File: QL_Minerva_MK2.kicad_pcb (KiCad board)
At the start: 2 copper layers, 41.9 x 44.5 mm, 16 parts, among them J1 Conn_01x02_Pin, J2 Conn_01x05_Pin, U1 Socket to QL, U2 W27C512, U3 PCF8583P, U4 GAL16V8, U5 74LS133, Y1 32.768 kHz

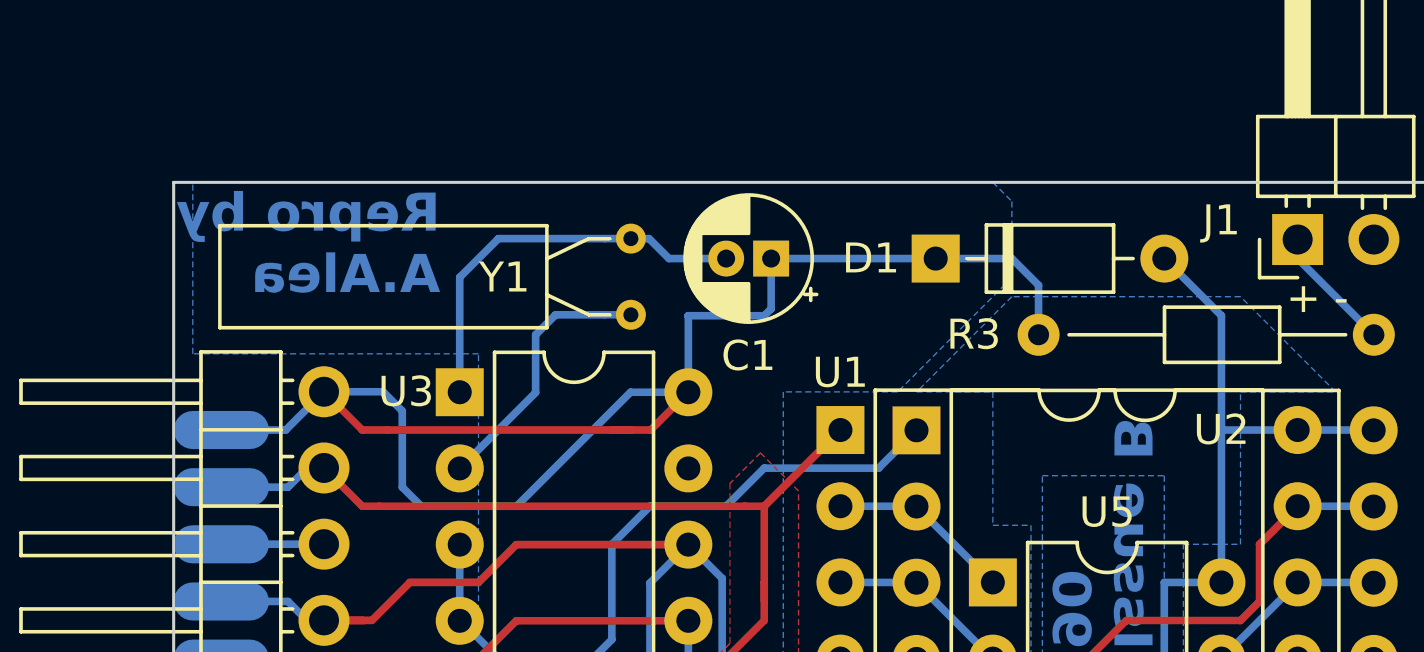
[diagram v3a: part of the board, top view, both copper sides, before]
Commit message: update C footprint
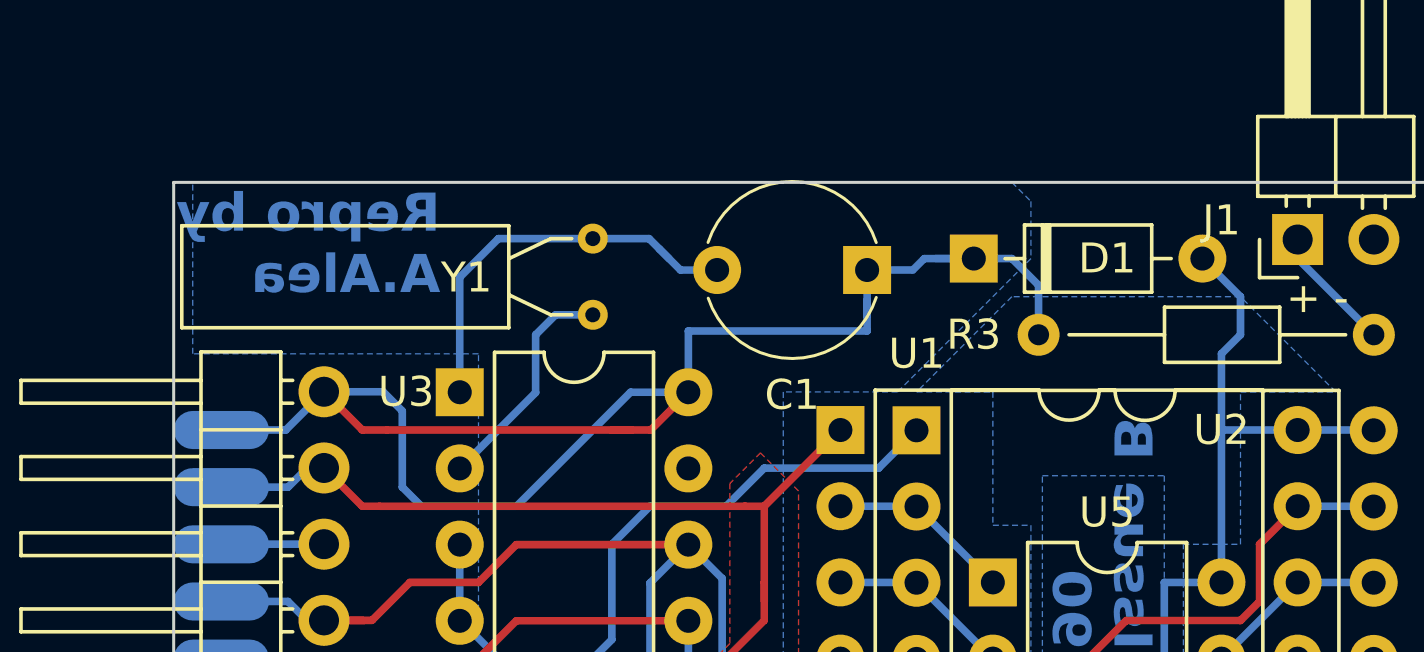
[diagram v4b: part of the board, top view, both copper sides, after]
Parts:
- C1: footprint Capacitor_THT:CP_Radial_D4.0mm_P1.50mm -> 8bits:C_Variable_Radial_D6.0mm_P5.00mm
- moved C1 3.22 mm to (80.3, 59.4)
- moved D1 1.27 mm to (83.8, 59.1)
- moved Y1 1.27 mm to (71.1, 58.4)
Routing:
- net /K: track 53.6 -> 55.3 mm
- net Net-(U3-X2): track 8.95 -> 7.68 mm

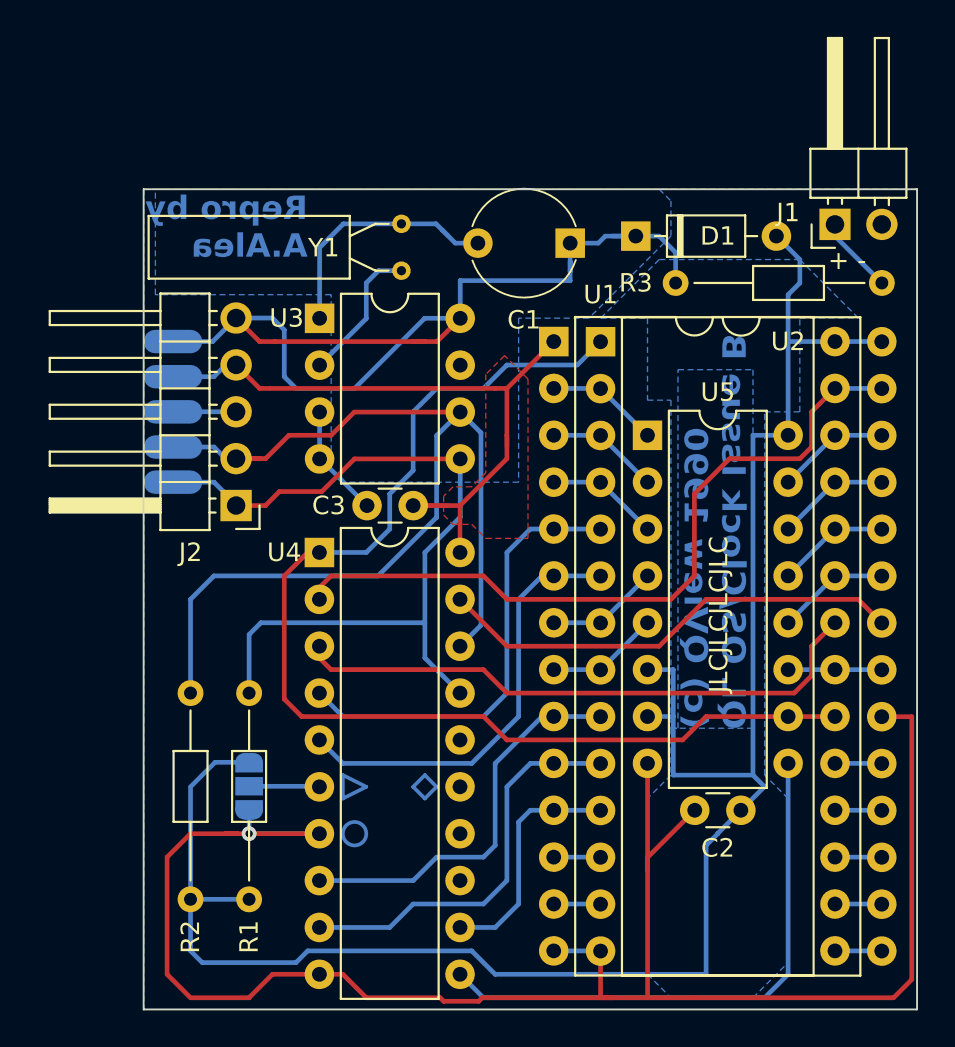
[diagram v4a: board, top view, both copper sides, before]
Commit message: fixed error in leg 7 of gal
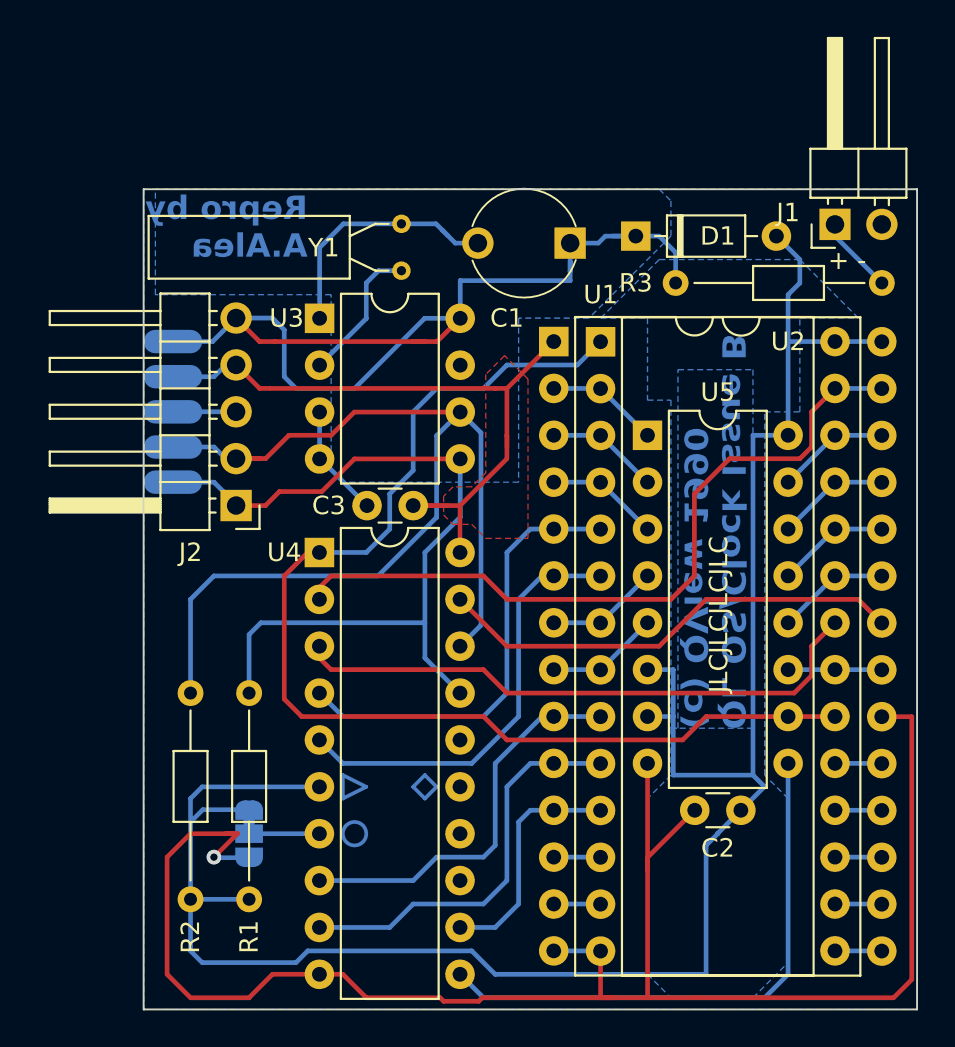
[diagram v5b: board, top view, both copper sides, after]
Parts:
- JP1: footprint Jumper:SolderJumper-3_P1.3mm_Open_RoundedPad1.0x1.5mm -> Jumper:SolderJumper-3_P1.3mm_Bridged12_RoundedPad1.0x1.5mm
- moved JP1 2.57 mm to (62.9, 91.4), turned to -90 degrees
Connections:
- JP1 pad 1: GND -> VCC
- JP1 pad 2: Net-(JP1-C) -> /DECODE
- JP1 pad 3: VCC -> GND
- U4 pad 11: /DECODE -> Net-(U4-I10/~{OE})
- U4 pad 6: Net-(JP1-C) -> VCC
- U4 pad 7: GND -> /DECODE
- U5 pad 9: /DECODE -> Net-(U4-I10/~{OE})
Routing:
- net Net-(U4-I10/~{OE}): track 0.00 -> 30.3 mm
- net /DECODE: track 30.3 -> 3.81 mm
- net VCC: track 107.0 -> 113.3 mm
- net GND: track 112.5 -> 106.6 mm
- net Net-(JP1-C): track 3.78 -> 0.00 mm

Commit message: Reduced size to avoid colision with cristal of QL Mainboard
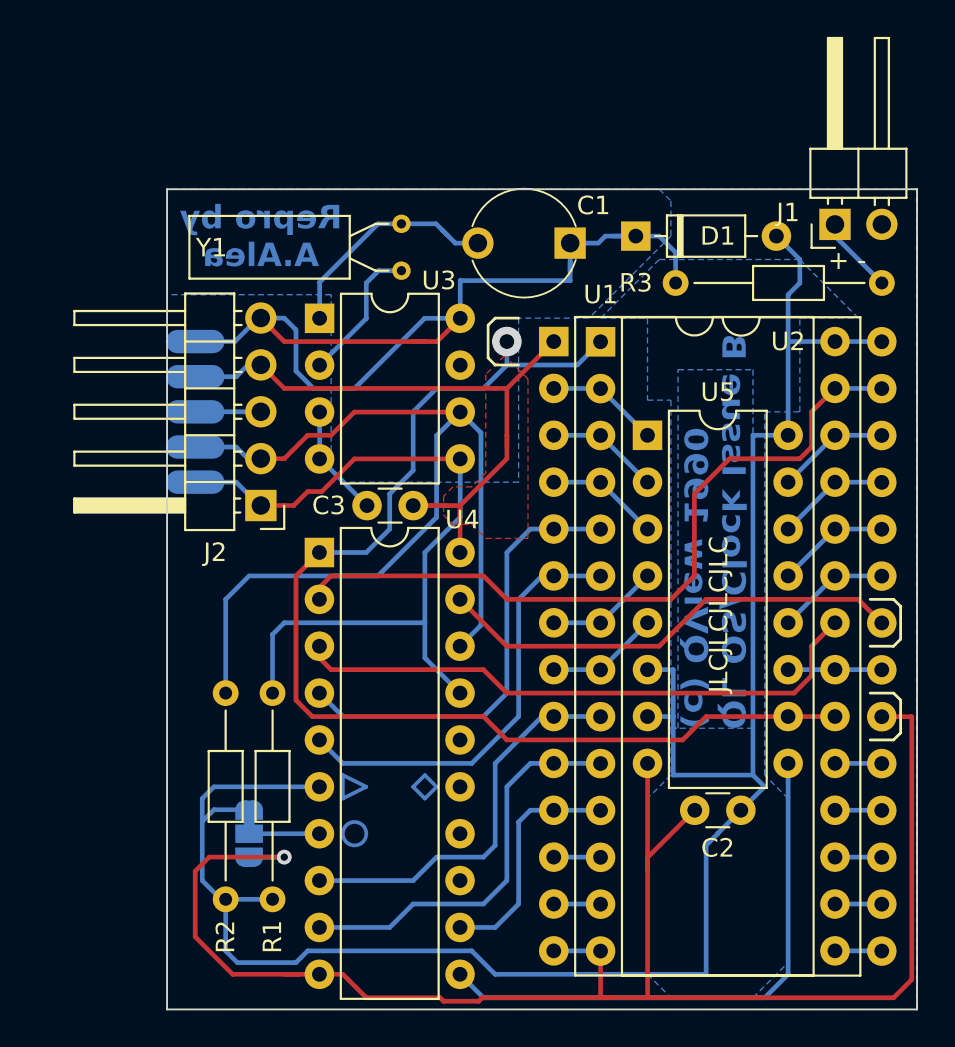
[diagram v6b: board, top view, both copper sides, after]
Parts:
- moved R2 1.91 mm to (61.6, 91.4)
- moved J2 1.34 mm to (63.5, 73.7)
- moved R1 1.27 mm to (64.1, 91.4)
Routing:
- net GND: track 106.6 -> 101.3 mm
- net /SCL: track 59.3 -> 54.1 mm
- net /K: track 55.3 -> 51.8 mm
- net /SDA: track 45.3 -> 42.1 mm
- net VCC: track 113.3 -> 110.2 mm
- net +5V: track 38.5 -> 37.2 mm
- net Net-(U3-OSCI): track 13.8 -> 12.7 mm
- net /A15: track 62.7 -> 63.4 mm, vias 0 -> 1
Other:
- board size 41.9 x 44.5 mm -> 40.6 x 44.5 mm
